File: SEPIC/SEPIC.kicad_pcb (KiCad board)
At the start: 2 copper layers, 41.7 x 57.8 mm, 15 parts, among them J1 Screw Terminal, J2 Barrel Jack, J3 Pin Header, J4 Screw Terminal, Q1 IRF520N, U1 HCPL-3120

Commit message: WIP: redimensionar componentes PCB
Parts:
- C1: footprint Capacitor_THT:C_Radial_D5.0mm_H11.0mm_P2.00mm -> Capacitor_THT:C_Radial_D10.0mm_H20.0mm_P5.00mm
- C2: value 22u -> 2.2u; footprint Capacitor_THT:C_Radial_D5.0mm_H11.0mm_P2.00mm -> Capacitor_THT:C_Rect_L16.5mm_W8.7mm_P15.00mm_MKT
- C4: footprint Capacitor_THT:C_Radial_D10.0mm_H12.5mm_P5.00mm -> Capacitor_THT:C_Radial_D16.0mm_H25.0mm_P7.50mm
- R1: footprint Resistor_THT:R_Axial_DIN0309_L9.0mm_D3.2mm_P12.70mm_Horizontal -> Resistor_THT:R_Axial_DIN0309_L9.0mm_D3.2mm_P2.54mm_Vertical
- moved C2 10.2 mm to (69.8, 47.8), turned to 180 degrees
- moved C1 6.52 mm to (50.2, 48.0), turned to 180 degrees
- moved Q1 4.38 mm to (80.5, 56.2)
- moved J3 3.13 mm to (80.1, 49.0)
- moved C4 2.01 mm to (66.7, 61.0)
- moved D1 1.98 mm to (70.8, 71.0)
- moved R1 0.88 mm to (67.5, 39.5)
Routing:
- net Net-(Q1-D): track 32.9 -> 0.00 mm
- net PWM: track 17.6 -> 12.5 mm
- net Net-(J3-Pin_2): track 12.5 -> 16.5 mm
- net VCC: track 1.77 -> 0.00 mm
- added copper zone on B.Cu, net (none)
- added copper zone on B.Cu, net Net-(Q1-D)
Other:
- board size 41.7 x 57.8 mm -> 42.7 x 57.8 mm
- board text added: "LOS PELELES"

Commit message: PCB aprobada por Seba
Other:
- board size 42.7 x 57.8 mm -> 43.7 x 57.8 mm
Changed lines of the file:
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@@
 	(gr_rect
 		(start 41.5 26.25)
-		(end 84.2 84)
+		(end 85.2 84)
 		(stroke
 			(width 0.05)
@@
 		)
 	)
-	(gr_text "LOS PELELES"
-		(at 74.2 52.8 0)
+	(gr_text "LOS\nPELELES"
+		(at 67.75 54.1 0)
 		(layer "B.Cu" knockout)
 		(effects
 			(font
-				(size 1.5 1.5)
-				(thickness 0.3)
-				(bold yes)
-			)
-			(justify left bottom mirror)
-		)
-	)
-	(segment
-		(start 82 47.38)
-		(end 82 53.95)
+				(size 2 2)
+				(thickness 0.4)
+			)
+			(justify mirror)
+		)
+	)
+	(segment
+		(start 81.8 54.15)
+		(end 80.5 55.45)
 		(width 0.8)
 		(layer "B.Cu")
@@
 	)
 	(segment
+		(start 79.87 45.25)
+		(end 81.8 47.18)
+		(width 0.8)
+		(layer "B.Cu")
+		(net 6)
+	)
+	(segment
 		(start 80.5 55.45)
-		(end 82 53.95)
+		(end 80.5 56.2)
 		(width 0.8)
 		(layer "B.Cu")
@@
 	)
 	(segment
-		(start 80.5 56.2)
-		(end 80.5 55.45)
-		(width 0.8)
-		(layer "B.Cu")
-		(net 6)
-	)
-	(segment
-		(start 79.87 45.25)
-		(end 82 47.38)
+		(start 81.8 47.18)
+		(end 81.8 54.15)
 		(width 0.8)
 		(layer "B.Cu")
@@
 		(polygon
 			(pts
-				(xy 62.6 40.8) (xy 62.6 37.4) (xy 69.6 37.4) (xy 69.6 35.2) (xy 80.4 35) (xy 80.2 32.4) (xy 74.6 32.4)
-				(xy 74.6 29) (xy 67.8 29) (xy 67.8 35.4) (xy 61.2 35.4) (xy 61.2 40.8)
+				(xy 62.6 40.8) (xy 62.6 38.25) (xy 63.45 37.4) (xy 69.6 37.4) (xy 69.6 35.25) (xy 80.25 35.25) (xy 80.25 32.4)
+				(xy 74.6 32.4) (xy 74.6 29) (xy 67.8 29) (xy 67.8 33.8) (xy 66.2 35.4) (xy 61.2 35.4) (xy 61.2 40.8)
+			)
+		)
+	)
+	(zone
+		(net 0)
+		(net_name "")
+		(layer "B.Cu")
+		(hatch edge 0.5)
+		(priority 1)
+		(connect_pads
+			(clearance 0.125)
+		)
+		(min_thickness 0.125)
+		(filled_areas_thickness no)
+		(fill yes
+			(thermal_gap 0.5)
+			(thermal_bridge_width 0.5)
+			(island_removal_mode 1)
+			(island_area_min 10)
+		)
+		(polygon
+			(pts
+				(xy 70 35.25) (xy 64.25 35.25) (xy 64.25 37.25) (xy 62.5 37.25) (xy 62.5 38.75) (xy 64.25 38.75)
+				(xy 64.25 43.25) (xy 69.75 43.25) (xy 69.75 43.75) (xy 77.25 51.25) (xy 81.5 51.25) (xy 81.5 43.3125)
+				(xy 81.1875 43) (xy 80.25 43) (xy 76.75 43) (xy 76.75 41.5) (xy 78.5 39.75) (xy 80.25 39.75) (xy 80.25 35.25)
 			)
 		)
@@
 		(polygon
 			(pts
-				(xy 41.5 26.25) (xy 84.25 26.25) (xy 84.25 84) (xy 41.5 84)
-			)
-		)
-	)
-	(zone
-		(net 0)
-		(net_name "")
-		(layer "B.Cu")
-		(hatch edge 0.5)
-		(priority 6)
-		(connect_pads
-			(clearance 0.5)
-		)
-		(min_thickness 0.25)
-		(filled_areas_thickness no)
-		(fill yes
-			(thermal_gap 0.5)
-			(thermal_bridge_width 0.5)
-			(island_removal_mode 1)
-			(island_area_min 10)
-		)
-		(polygon
-			(pts
-				(xy 73 41.5) (xy 78 38.5) (xy 78 39.5) (xy 76.5 41) (xy 76.5 44.5) (xy 80 46.5) (xy 80 48.5) (xy 76 48.5)
-				(xy 73 45.5)
+				(xy 41.5 26.25) (xy 85.25 26.25) (xy 85.25 84) (xy 41.5 84)
 			)
 		)
@@
 		(layer "B.Cu")
 		(hatch edge 0.5)
-		(priority 4)
+		(priority 7)
 		(connect_pads yes
 			(clearance 0.5)
@@
 		(polygon
 			(pts
-				(xy 71.8 59.2) (xy 65.8 59.2) (xy 65.2 59.8) (xy 65.2 75.8) (xy 64.6 76.4) (xy 63.8 76.4) (xy 63.2 77)
-				(xy 63.2 80) (xy 63.8 80.6) (xy 68 80.6) (xy 68.6 80) (xy 68.6 73.8) (xy 69.2 73.2) (xy 71.8 73.2)
-				(xy 72.4 72.6) (xy 72.4 59.8)
+				(xy 66.6 59.2) (xy 65.2 60.6) (xy 65.2 75.6) (xy 64.6 76.4) (xy 63.8 76.4) (xy 63.2 77) (xy 63.2 80)
+				(xy 63.8 80.6) (xy 68 80.6) (xy 68.6 80) (xy 68.6 73.8) (xy 69.2 73.2) (xy 71.8 73.2) (xy 72.4 72.6)
+				(xy 72.4 63) (xy 72.05 63) (xy 72.05 60.15) (xy 71.05 59.2)
 			)
 		)
@@
 		(polygon
 			(pts
-				(xy 46.546485 38) (xy 57.396485 38) (xy 57.396485 39.2) (xy 64.296485 39.2) (xy 64.296485 45.4)
-				(xy 52.419003 45.4) (xy 52.546485 61.5) (xy 50.046485 61.5) (xy 46.546485 61.5)
+				(xy 46.546485 38) (xy 57.171485 38) (xy 57.396485 38.225) (xy 57.396485 38.9) (xy 57.696485 39.2)
+				(xy 64.296485 39.2) (xy 64.296485 43.85) (xy 62.646485 45.5) (xy 54.901662 45.5) (xy 52.439446 47.981789)
+				(xy 52.541536 60.87502) (xy 51.921485 61.5) (xy 50.046485 61.5) (xy 47.421485 61.5) (xy 46.546485 60.625)
 			)
 		)
@@
 		(polygon
 			(pts
-				(xy 53 43.6) (xy 53 62.2) (xy 65 62.2) (xy 65 60) (xy 82 60) (xy 82 43.6)
-			)
-		)
+				(xy 68.75 43.6) (xy 56.6 43.6) (xy 56.6 62.4) (xy 65.2 62.4) (xy 65.2 60.6) (xy 72.25 60.6) (xy 72.25 59.55)
+				(xy 73.4 58.4) (xy 75.15 58.4) (xy 76.15 59.4) (xy 76.15 59.8) (xy 76.35 60) (xy 82 60) (xy 82 51.75)
+				(xy 77 51.75)
+			)
+		)

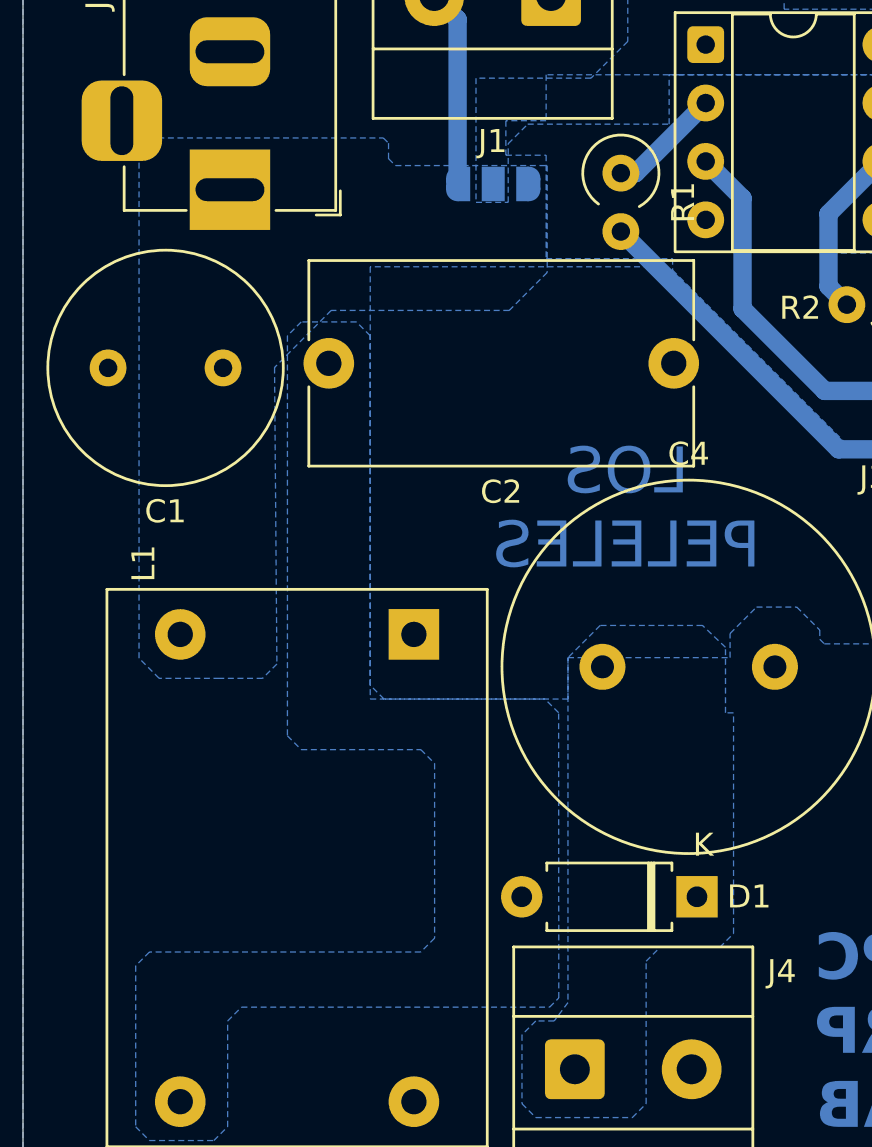
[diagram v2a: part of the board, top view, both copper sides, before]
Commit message: Agregar testpoints corriente PCB
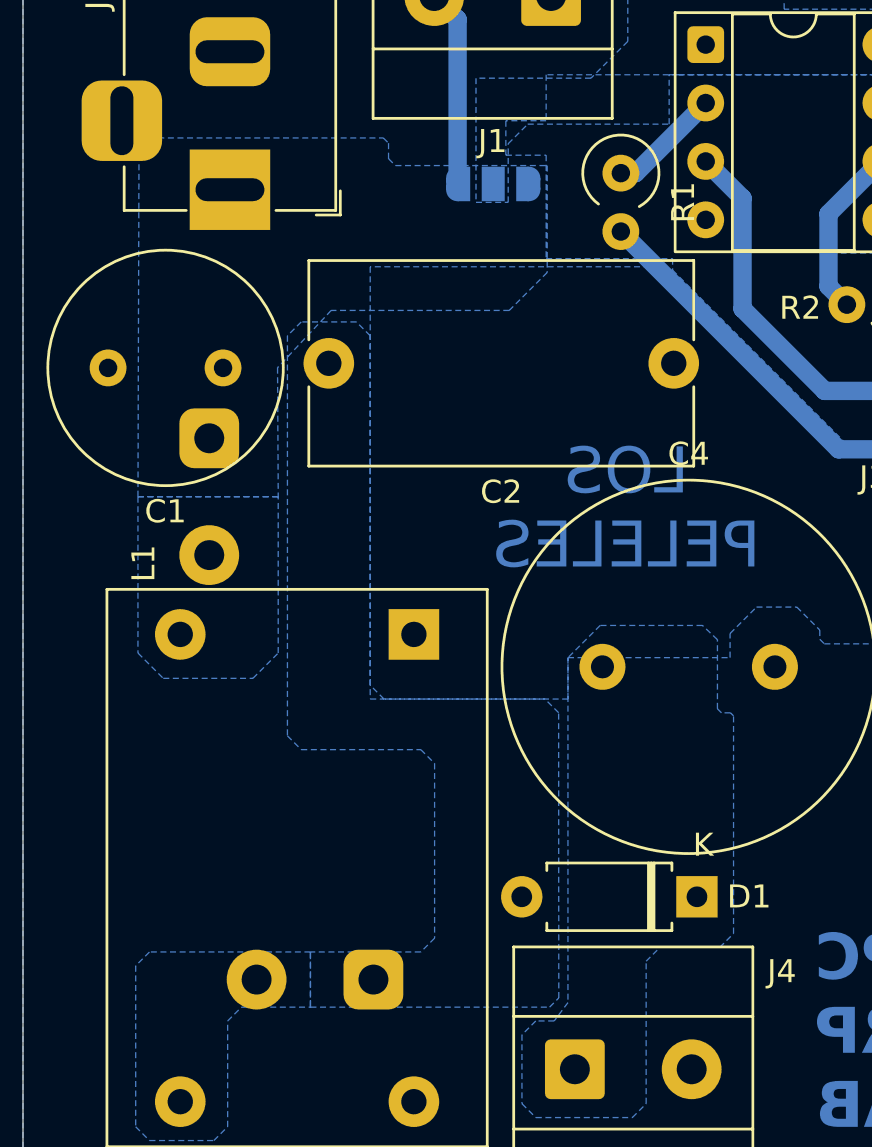
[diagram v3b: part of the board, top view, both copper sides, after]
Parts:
- added TP1: Shunt, TestPoint:TestPoint_2Pads_Pitch5.08mm_Drill1.3mm, B.Cu at (49.6, 51.1)
- added TP2: Shunt, TestPoint:TestPoint_2Pads_Pitch5.08mm_Drill1.3mm, B.Cu at (56.7, 74.6)
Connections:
- L1 pad 2: +24V -> Net-(L1-Pad2)
- L1 pad 3: Net-(D1-A) -> Net-(L1-Pad3)
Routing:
- added copper zone on B.Cu, net Net-(L1-Pad2)
- added copper zone on B.Cu, net Net-(L1-Pad3)

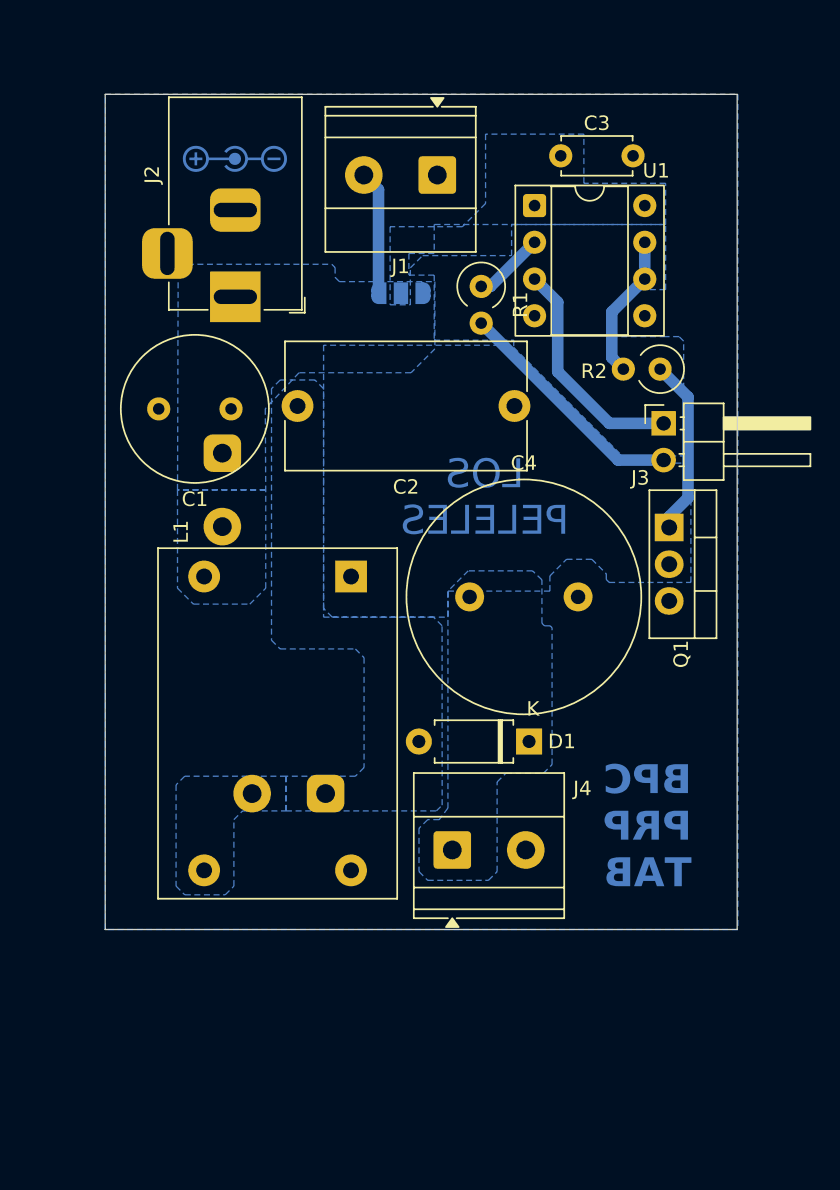
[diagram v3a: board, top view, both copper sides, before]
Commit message: Agregar puntos medición corriente
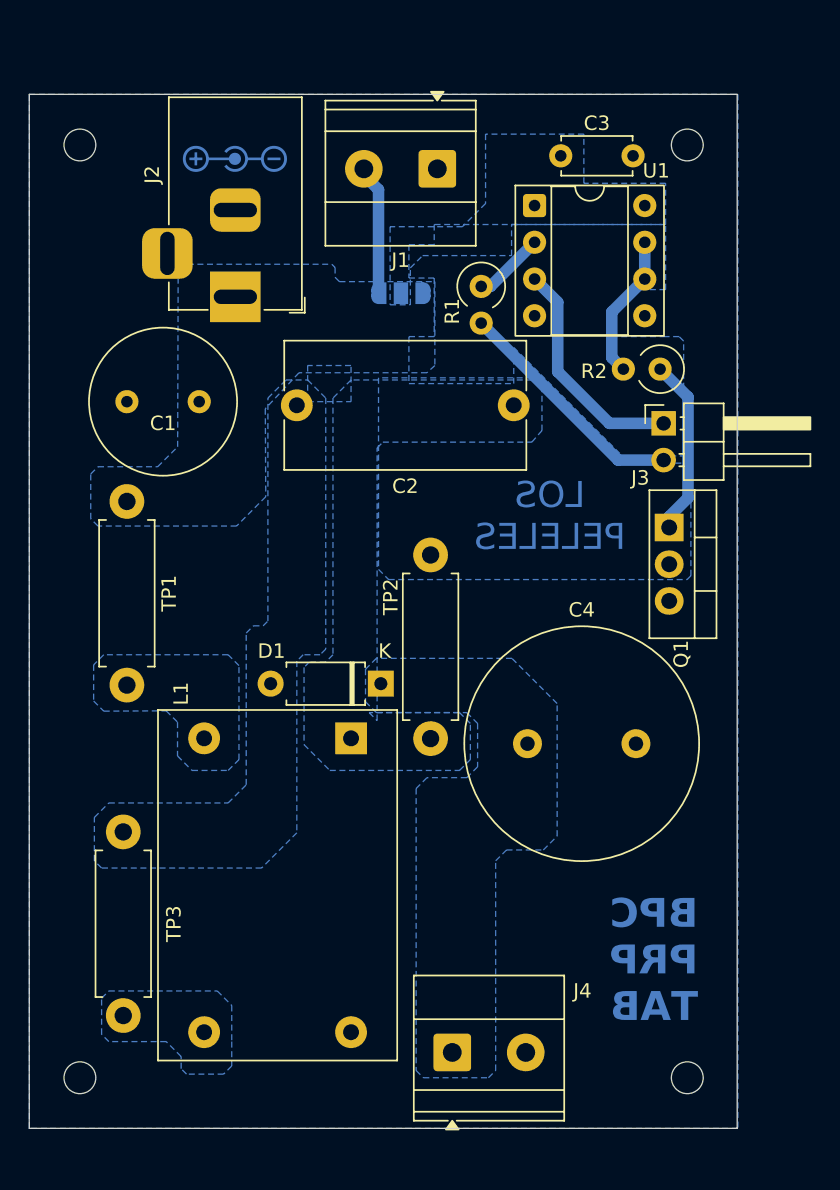
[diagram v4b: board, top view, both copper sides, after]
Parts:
- added REF**: MountingHole_2.2mm_M2, MountingHole:MountingHole_2.2mm_M2, F.Cu at (39.8, 29.8)
- added REF**: MountingHole_2.2mm_M2, MountingHole:MountingHole_2.2mm_M2, F.Cu at (81.8, 29.8)
- added REF**: MountingHole_2.2mm_M2, MountingHole:MountingHole_2.2mm_M2, F.Cu at (39.8, 94.2)
- added REF**: MountingHole_2.2mm_M2, MountingHole:MountingHole_2.2mm_M2, F.Cu at (81.8, 94.2)
- added TP2: Shunt, Resistor_THT:R_Axial_DIN0411_L9.9mm_D3.6mm_P12.70mm_Horizontal, F.Cu at (64.0, 70.8)
- R2: value 0 -> 6
- TP1: footprint TestPoint:TestPoint_2Pads_Pitch5.08mm_Drill1.3mm -> Resistor_THT:R_Axial_DIN0411_L9.9mm_D3.6mm_P12.70mm_Horizontal; moved to F.Cu
- TP3: renamed from TP2; footprint TestPoint:TestPoint_2Pads_Pitch5.08mm_Drill1.3mm -> Resistor_THT:R_Axial_DIN0411_L9.9mm_D3.6mm_P12.70mm_Horizontal; moved to F.Cu
- moved TP3 14.2 mm to (42.8, 77.2), turned to -90 degrees
- moved J4 14.0 mm to (65.5, 92.5)
- moved L1 11.2 mm to (58.5, 70.8)
- moved D1 11.0 mm to (60.6, 67.0)
- moved C4 10.9 mm to (70.7, 71.2)
- moved TP1 7.40 mm to (43.0, 54.4)
- moved C1 2.26 mm to (48.0, 47.5)
- moved J1 0.43 mm to (64.5, 31.4)
- moved C2 0.07 mm to (69.8, 47.8)
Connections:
- C2 pad 1: Net-(Q1-D) -> Net-(C2-Pad1)
- L1 pad 1: Net-(Q1-D) -> Net-(C2-Pad1)
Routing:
- added copper zone on B.Cu, net Net-(C2-Pad1)
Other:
- board size 43.7 x 57.8 mm -> 49 x 71.5 mm

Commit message: Condensadores salida
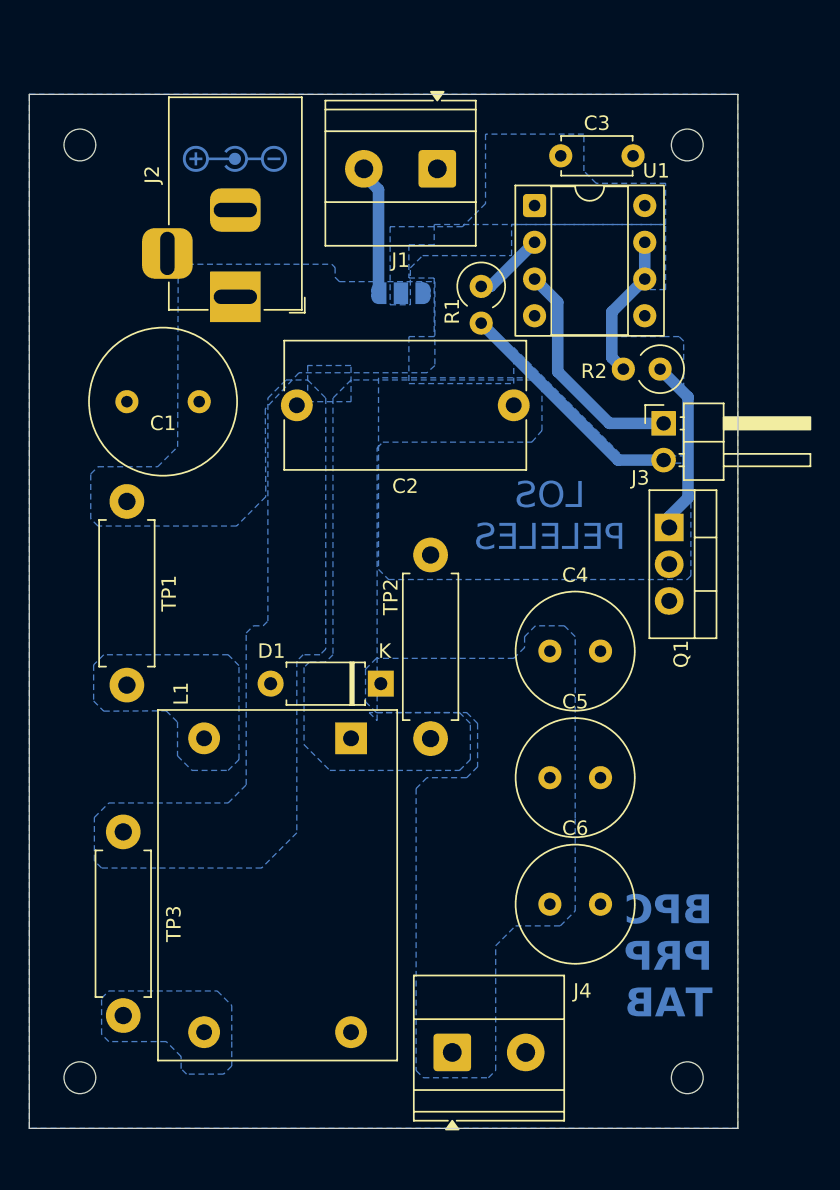
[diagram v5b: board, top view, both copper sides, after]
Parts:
- added C5: 10u, Capacitor_THT:C_Radial_D8.0mm_H11.5mm_P3.50mm, F.Cu at (72.2, 73.5)
- added C6: 10u, Capacitor_THT:C_Radial_D8.0mm_H11.5mm_P3.50mm, F.Cu at (72.2, 82.2)
- C4: value 220u -> 10u; footprint Capacitor_THT:C_Radial_D16.0mm_H25.0mm_P7.50mm -> Capacitor_THT:C_Radial_D8.0mm_H11.5mm_P3.50mm
- D1: value SR502 -> SR5200
- moved C4 6.59 mm to (72.2, 64.8)
